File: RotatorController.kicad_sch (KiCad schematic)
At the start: 59 parts, among them J1 USB_A, J2 26 VAC, J3 Rotator, J4 Motor Cap, K1 G5LE-1, K2 G5LE-1, K3 G5LE-1, Q1 BSS123, Q2 BSS123, Q3 BSS123, SW1 SW_CW, SW2 SW_CCW, U1 Teensy4.0, U3 AP2161W

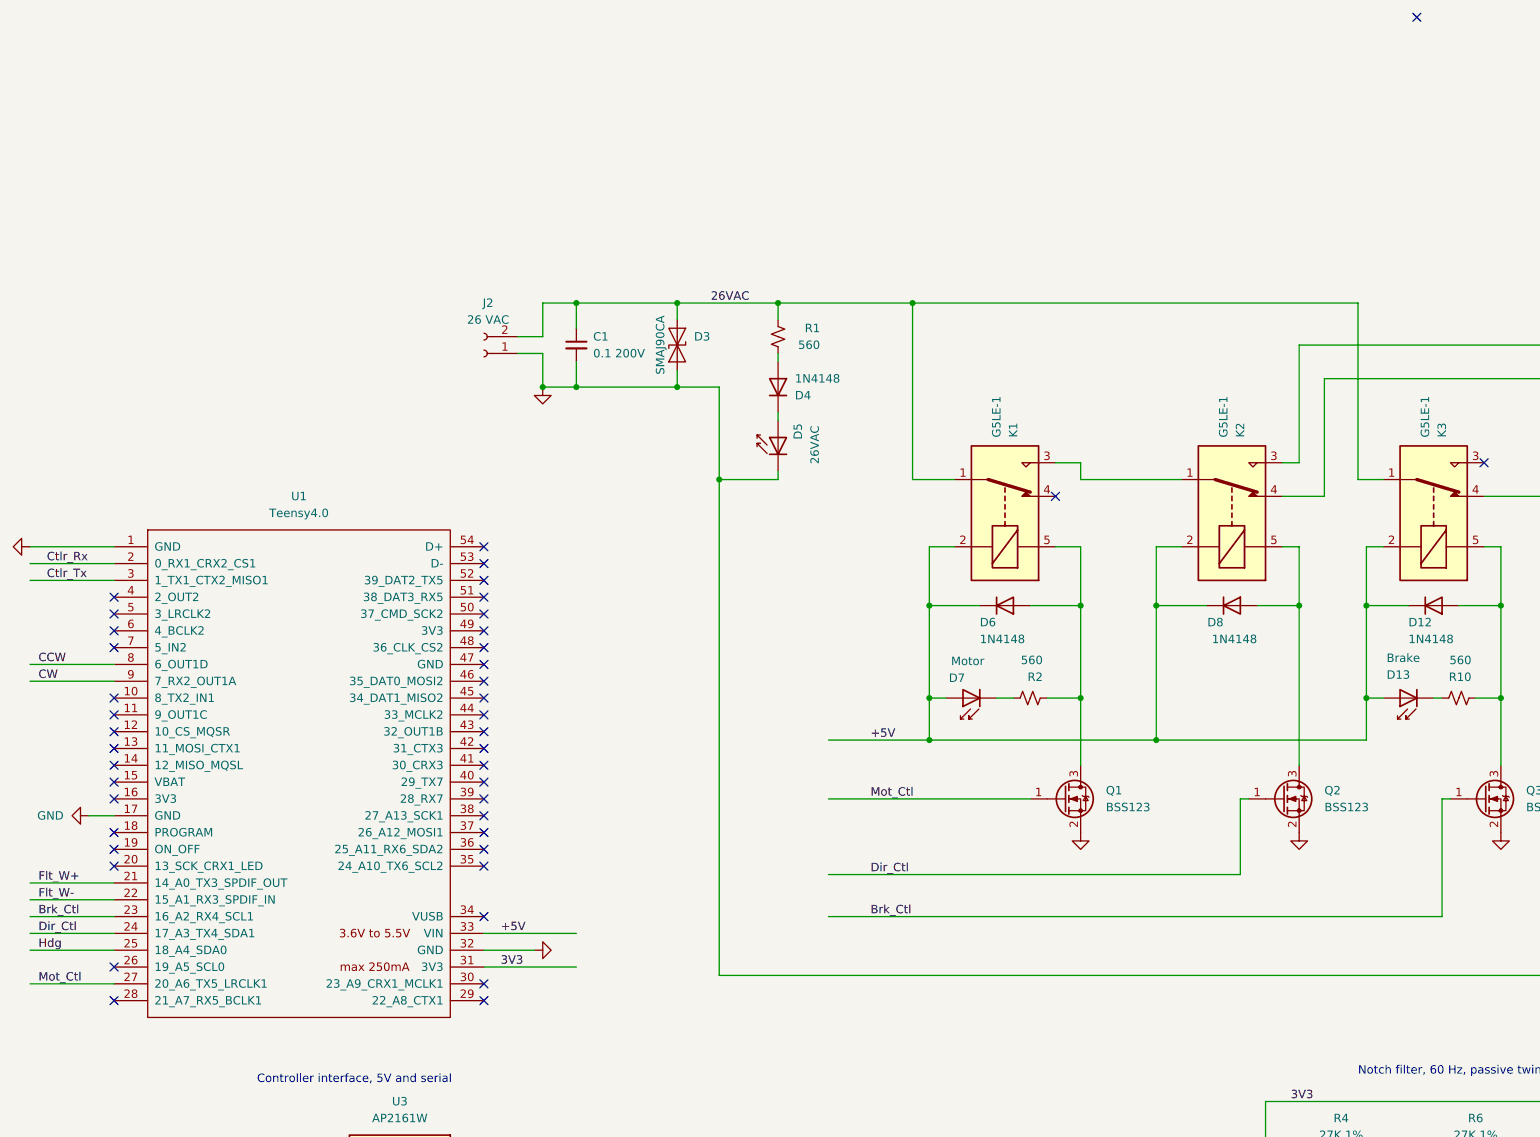
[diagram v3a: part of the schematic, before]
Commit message: Simplified symbol and footprint for Teensy4.0 to remove unused pins Corrected error where footprints reverted to through-hole (mystery)
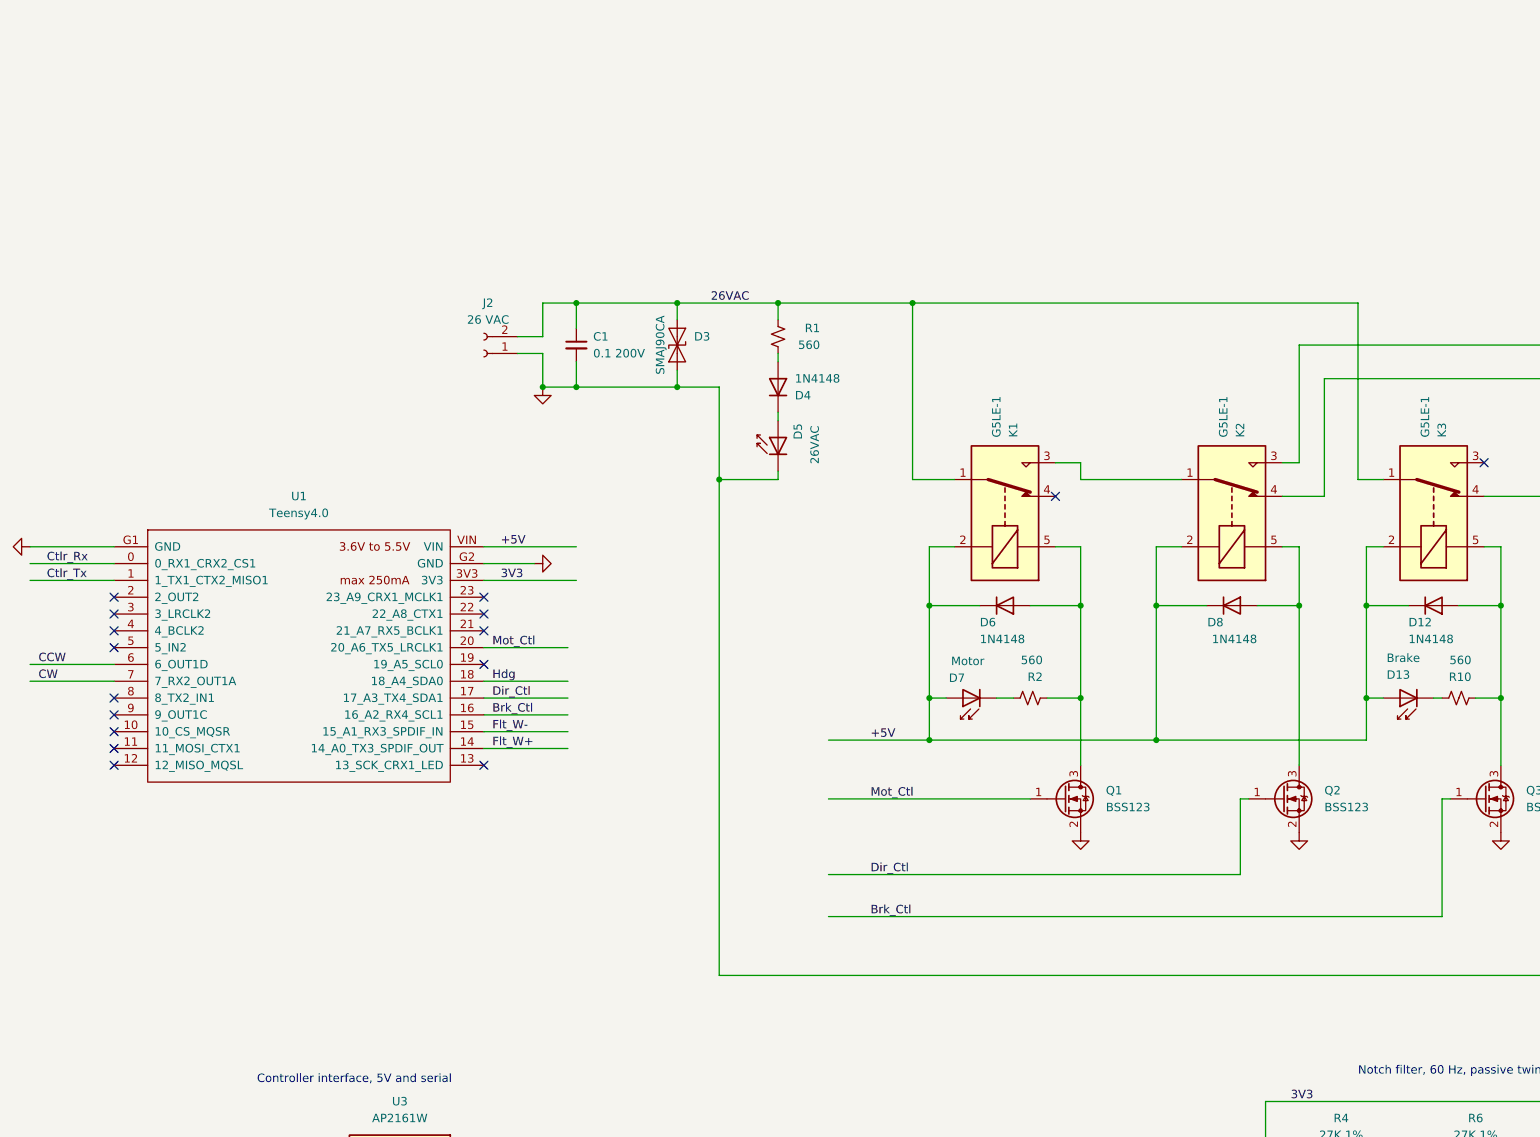
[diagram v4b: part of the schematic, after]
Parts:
- D13, D19, D5, D7: footprint LED_SMD:LED_0603_1608Metric_Pad1.05x0.95mm_HandSolder -> LED_SMD:LED_miniPLCC_2315_Handsoldering
- U1: footprint Teensy:Teensy40 -> Teensy:Teensy40_Simple; symbol Teensy:Teensy4.0 -> Teensy:Teensy4.0_Simple
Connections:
- net +5V: now also U1.VIN; no longer U1.33 (VIN)
- net 3V3: now also U1.3V3; no longer U1.31 (3V3)
- net Brk_Ctl: now also U1.16 (16_A2_RX4_SCL1); no longer U1.23 (16_A2_RX4_SCL1)
- net CCW: now also U1.6 (6_OUT1D); no longer U1.8 (6_OUT1D)
- net CW: now also U1.7 (7_RX2_OUT1A); no longer U1.9 (7_RX2_OUT1A)
- net Ctlr_Rx: now also U1.0 (0_RX1_CRX2_CS1); no longer U1.2 (0_RX1_CRX2_CS1)
- net Ctlr_Tx: now also U1.1 (1_TX1_CTX2_MISO1); no longer U1.3 (1_TX1_CTX2_MISO1)
- net Dir_Ctl: now also U1.17 (17_A3_TX4_SDA1); no longer U1.24 (17_A3_TX4_SDA1)
- net Flt_W+: now also U1.14 (14_A0_TX3_SPDIF_OUT); no longer U1.21 (14_A0_TX3_SPDIF_OUT)
- net Flt_W-: now also U1.15 (15_A1_RX3_SPDIF_IN); no longer U1.22 (15_A1_RX3_SPDIF_IN)
- net GND: now also U1.G1 (GND), U1.G2 (GND); no longer U1.1 (GND), U1.17 (GND), U1.32 (GND)
- net Hdg: now also U1.18 (18_A4_SDA0); no longer U1.25 (18_A4_SDA0)
- net Mot_Ctl: now also U1.20 (20_A6_TX5_LRCLK1); no longer U1.27 (20_A6_TX5_LRCLK1)
- no-connect marks 43 -> 17

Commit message: Board dimensions in inches tweaked layout
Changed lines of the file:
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@@
     (stroke (width 0) (type default))
   )
-  (wire (pts (xy 19.05 69.85) (xy 31.75 69.85))
+  (wire (pts (xy 21.59 69.85) (xy 31.75 69.85))
     (stroke (width 0) (type default))
   )
@@
     (effects (font (size 1.27 1.27)) (justify left bottom))
   )
-  (text "Lightpipe 4 high" (at 382.27 229.87 0)
+  (text "Lightpipe 4 high" (at 267.97 102.87 0)
     (effects (font (size 1.27 1.27)) (justify left bottom))
   )
@@
     )
   )
-  (symbol (lib_id "power:GND") (at 19.05 69.85 270) (unit 1)
-    (in_bom yes) (on_board yes) (dnp no) (fields_autoplaced)
-    (property "Reference" "#PWR01" (at 12.7 69.85 0)
-      (effects (font (size 1.27 1.27)) hide)
-    )
-    (property "Value" "GND" (at 15.24 69.85 90)
+  (symbol (lib_id "power:GND") (at 21.59 69.85 270) (unit 1)
+    (in_bom yes) (on_board yes) (dnp no) (fields_autoplaced)
+    (property "Reference" "#PWR01" (at 15.24 69.85 0)
+      (effects (font (size 1.27 1.27)) hide)
+    )
+    (property "Value" "GND" (at 17.78 69.85 90)
       (effects (font (size 1.27 1.27)) (justify right) hide)
     )
-    (property "Footprint" "" (at 19.05 69.85 0)
-      (effects (font (size 1.27 1.27)) hide)
-    )
-    (property "Datasheet" "" (at 19.05 69.85 0)
-      (effects (font (size 1.27 1.27)) hide)
-    )
+    (property "Footprint" "" (at 21.59 69.85 0)
+      (effects (font (size 1.27 1.27)) hide)
+    )
+    (property "Datasheet" "" (at 21.59 69.85 0)
+      (effects (font (size 1.27 1.27)) hide)
+    )

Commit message: Homing in on final release add ground to pot and button mounting pads added start of dimensions and front panel sketch
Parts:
- removed J2: 26 VAC, Connector_TE-Connectivity:TE_MATE-N-LOK_1-770966-x_1x02_P4.14mm_Horizontal, symbol Connector:Conn_01x02_Socket
- removed J3: Rotator, Connector_TE-Connectivity:TE_MATE-N-LOK_1-770970-x_2x04_P4.14mm_Horizontal, symbol Connector:Conn_01x08_Socket
- added J2: Rotator, Connector_TE-Connectivity:TE_MATE-N-LOK_1-770971-x_2x05_P4.14mm_Horizontal, symbol Connector:Conn_01x10_Socket
- R1: value 560 -> 1000
- RV1: value R_Potentiometer_US -> Az_Preset
- SW1: value SW_CW -> CW
- SW2: value SW_CCW -> CCW
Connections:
- net 26VAC: now also J2.1 (Pin_1)
- net Brake: now also J2.2 (Pin_2)
- net Cap1: now also J2.9 (Pin_9)
- net Cap2: now also J2.5 (Pin_5)
- net GND: now also J2.10 (Pin_10), J2.6 (Pin_6)
- net Left: now also J2.7 (Pin_7)
- net Right: now also J2.3 (Pin_3)
- net Wiper+: now also J2.4 (Pin_4)
- net Wiper-: now also J2.8 (Pin_8)
- net Hdg renamed AzPre
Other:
- moved on the sheet: C1, C11, C12, C2, C3, C4, C5, C6, C7, C8, C9, D10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

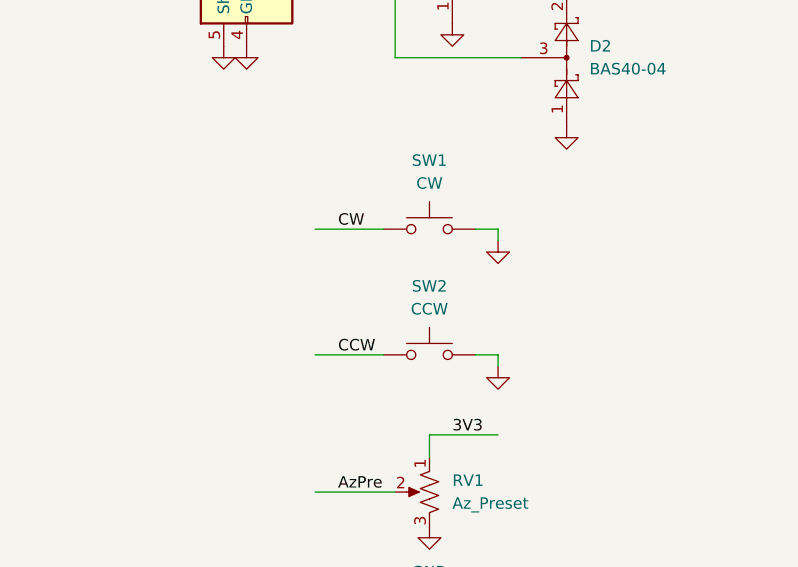
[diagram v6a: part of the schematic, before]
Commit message: fine tuned layout to shorten bypass cap ground and to reduce ground plane breaks
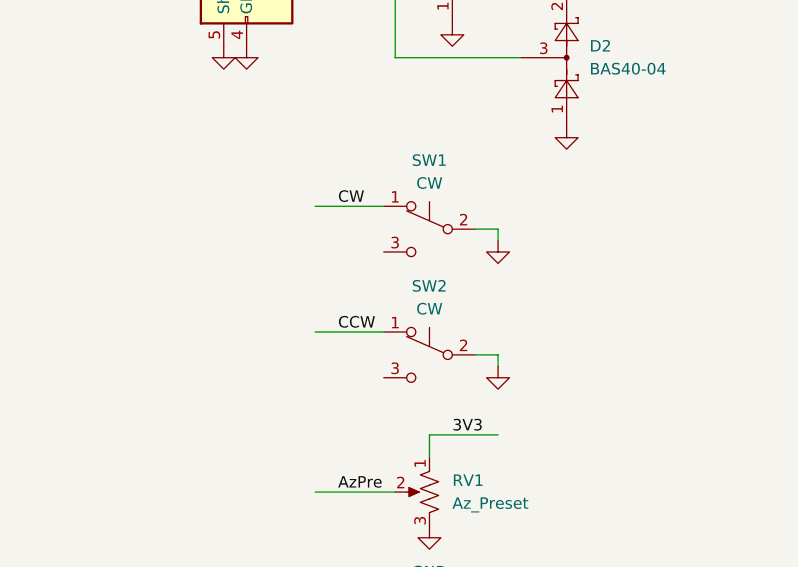
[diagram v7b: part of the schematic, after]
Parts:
- removed SW2: CCW, Button_Switch_THT:SW_SPST_Omron_B3F-315x_Angled, symbol Switch:SW_Push
- added SW2: CW, Button_Switch_THT:SW_SPST_Omron_B3F-315x_Angled, symbol Switch:SW_Push_SPDT
- SW1: symbol Switch:SW_Push -> Switch:SW_Push_SPDT
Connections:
- net CCW: now also SW2.1 (A)
- net GND: now also SW2.2 (B)
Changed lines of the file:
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@@
     (stroke (width 0) (type default))
   )
-  (wire (pts (xy 52.07 213.36) (xy 59.69 213.36))
+  (wire (pts (xy 52.07 210.82) (xy 59.69 210.82))
     (stroke (width 0) (type default))
   )
@@
     (stroke (width 0) (type default))
   )
-  (wire (pts (xy 52.07 227.33) (xy 59.69 227.33))
+  (wire (pts (xy 52.07 224.79) (xy 59.69 224.79))
     (stroke (width 0) (type default))
   )
@@
     (effects (font (size 1.27 1.27)) (justify left bottom))
   )
-  (label "CCW" (at 54.61 227.33 0) (fields_autoplaced)
+  (label "CCW" (at 54.61 224.79 0) (fields_autoplaced)
     (effects (font (size 1.27 1.27)) (justify left bottom))
   )
@@
     (effects (font (size 1.27 1.27)) (justify left bottom))
   )
-  (label "CW" (at 54.61 213.36 0) (fields_autoplaced)
+  (label "CW" (at 54.61 210.82 0) (fields_autoplaced)
     (effects (font (size 1.27 1.27)) (justify left bottom))
   )
@@
     )
   )
-  (symbol (lib_id "Switch:SW_Push") (at 64.77 213.36 0) (unit 1)
-    (in_bom yes) (on_board yes) (dnp no) (fields_autoplaced)
+  (symbol (lib_id "Switch:SW_Push_SPDT") (at 64.77 213.36 0) (mirror y) (unit 1)
+    (in_bom yes) (on_board yes) (dnp no)
     (property "Reference" "SW1" (at 64.77 205.74 0)
       (effects (font (size 1.27 1.27)))
@@
       (effects (font (size 1.27 1.27)))
     )
-    (property "Footprint" "Button_Switch_THT:SW_SPST_Omron_B3F-315x_Angled" (at 64.77 208.28 0)
-      (effects (font (size 1.27 1.27)) hide)
-    )
-    (property "Datasheet" "~" (at 64.77 208.28 0)
-      (effects (font (size 1.27 1.27)) hide)
-    )
-    (pin "1")
-    (pin "2")
+    (property "Footprint" "Button_Switch_THT:SW_SPST_Omron_B3F-315x_Angled" (at 64.77 213.36 0)
+      (effects (font (size 1.27 1.27)) hide)
+    )
+    (property "Datasheet" "~" (at 64.77 213.36 0)
+      (effects (font (size 1.27 1.27)) hide)
+    )
+    (pin "1")
+    (pin "2")
+    (pin "3")
     (instances
       (project "RotatorController"
         (path "/9538e4ed-27e6-4c37-b989-9859dc0d49e8"
           (reference "SW1") (unit 1)
+        )
+      )
+    )
+  )
+  (symbol (lib_id "Switch:SW_Push_SPDT") (at 64.77 227.33 0) (mirror y) (unit 1)
+    (in_bom yes) (on_board yes) (dnp no)
+    (property "Reference" "SW2" (at 64.77 219.71 0)
+      (effects (font (size 1.27 1.27)))
+    )
+    (property "Value" "CW" (at 64.77 222.25 0)
+      (effects (font (size 1.27 1.27)))
+    )
+    (property "Footprint" "Button_Switch_THT:SW_SPST_Omron_B3F-315x_Angled" (at 64.77 227.33 0)
+      (effects (font (size 1.27 1.27)) hide)
+    )
+    (property "Datasheet" "~" (at 64.77 227.33 0)
+      (effects (font (size 1.27 1.27)) hide)
+    )
+    (pin "1")
+    (pin "2")
+    (pin "3")
+    (instances
+      (project "RotatorController"
+        (path "/9538e4ed-27e6-4c37-b989-9859dc0d49e8"
+          (reference "SW2") (unit 1)
         )
       )
@@
         )
       )
-    )
-  )
-  (symbol (lib_id "Switch:SW_Push") (at 64.77 227.33 0) (unit 1)
-    (in_bom yes) (on_board yes) (dnp no) (fields_autoplaced)
-    (property "Reference" "SW2" (at 64.77 219.71 0)
-      (effects (font (size 1.27 1.27)))
-    )
-    (property "Value" "CCW" (at 64.77 222.25 0)
-      (effects (font (size 1.27 1.27)))
-    )
-    (property "Footprint" "Button_Switch_THT:SW_SPST_Omron_B3F-315x_Angled" (at 64.77 222.25 0)
-      (effects (font (size 1.27 1.27)) hide)
-    )
-    (property "Datasheet" "~" (at 64.77 222.25 0)
-      (effects (font (size 1.27 1.27)) hide)
-    )
-    (pin "1")
-    (pin "2")
-    (instances
-      (project "RotatorController"
-        (path "/9538e4ed-27e6-4c37-b989-9859dc0d49e8"
-          (reference "SW2") (unit 1)
-        )
-      )
